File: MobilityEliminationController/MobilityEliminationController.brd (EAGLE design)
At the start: 57.1 x 63.5 mm, 97 parts, among them J11 M10X2, Q1 INFINEON_2N7002_DW, Q2 INFINEON_2N7002_DW, Q3 BS250F, Q4 BS250F, Q5 INFINEON_2N7002_DW, Q6 INFINEON_2N7002_DW, Q7 INFINEON_2N7002_DW, U1 MSP430F5521/5/7/9_PN80, U2 LTV-817, U3 SN74LV74, U4 SN74LV08

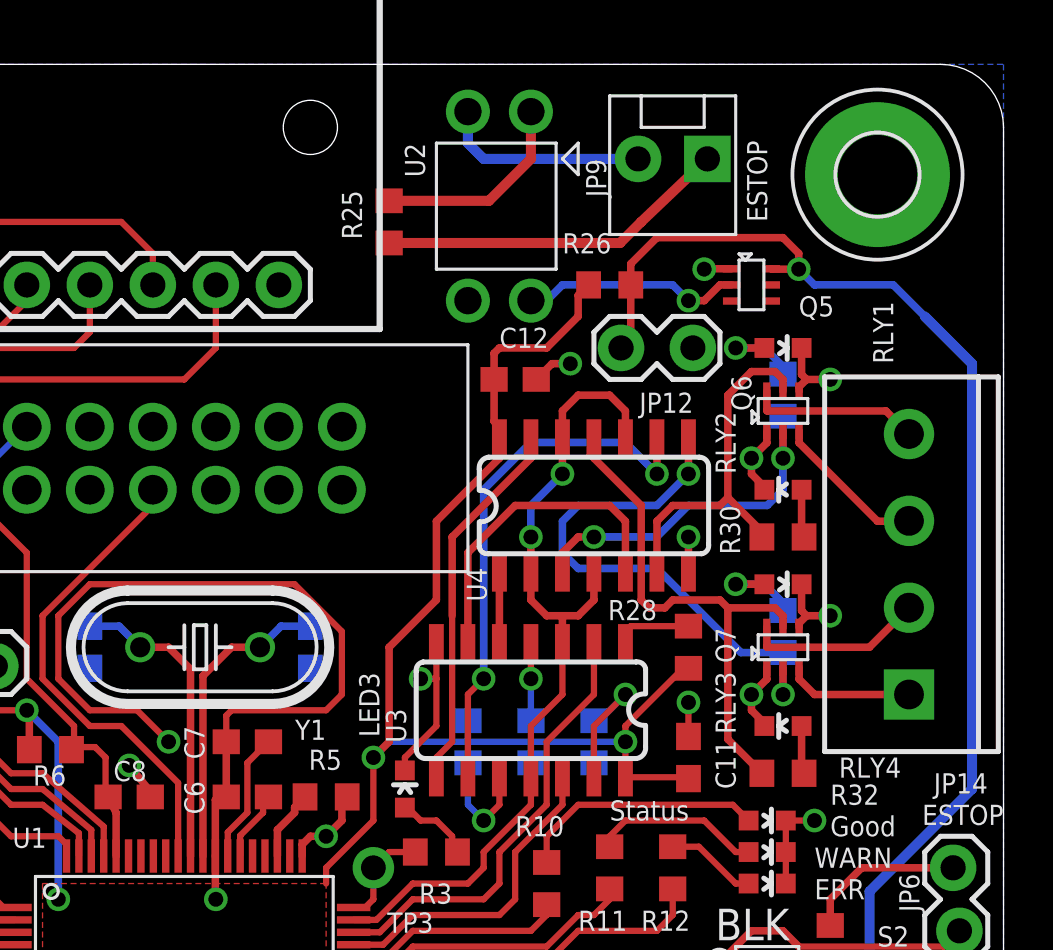
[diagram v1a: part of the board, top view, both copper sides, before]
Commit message: Power Controller, Elim-Mobility Controller, and PC2CAN sent to FAB
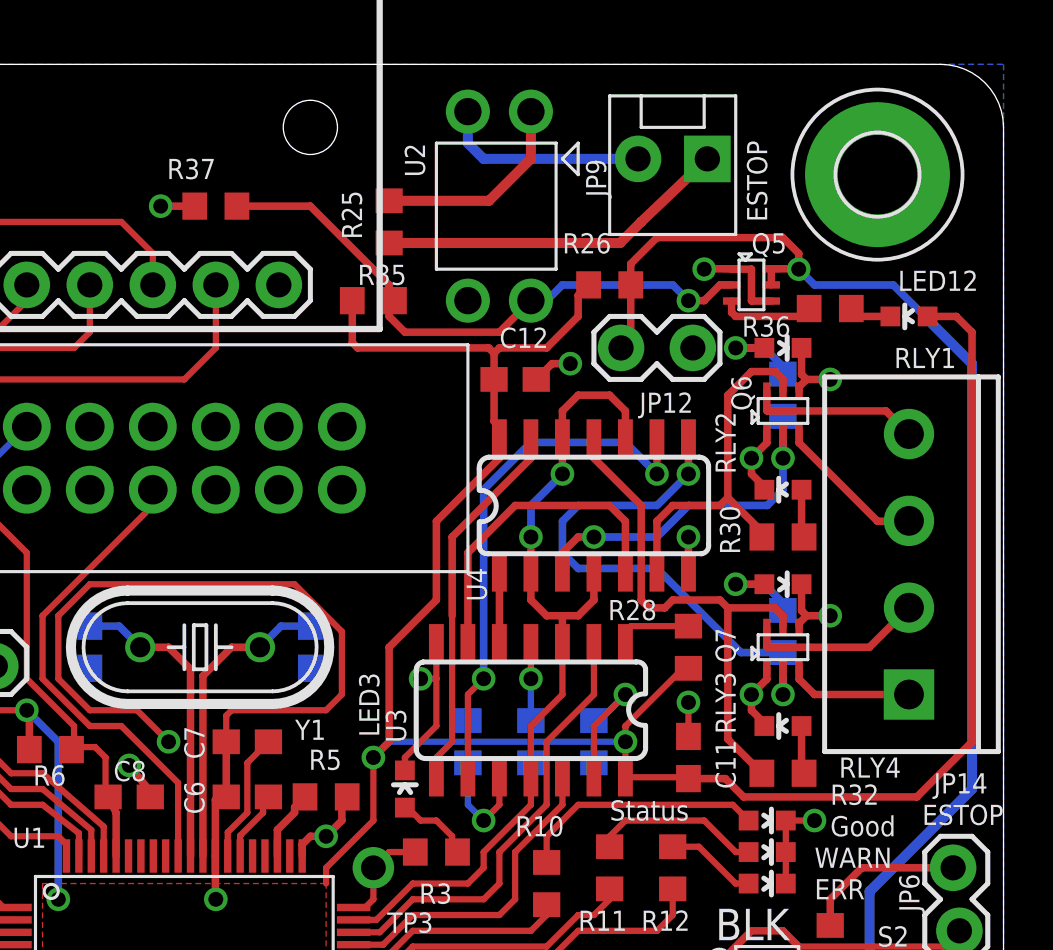
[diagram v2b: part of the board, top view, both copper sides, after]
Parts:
- added LED12: (no value), SparkFun-LED:LED-0603
- added R35: 10k, rcl:R0603
- added R36: 330, rcl:R0603
- added R37: 10M, rcl:R0603
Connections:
- new net N$15: Q5.3, R36.2
- new net N$16: LED12.C, R36.1
- net +3V3: now also LED12.A, R35.1
- net ESTOP_LOCAL: now also Q5.5
- net ESTOP_LOCAL_INV: now also R35.2, R37.1
- net GND: now also Q5.4, R37.2
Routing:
- net +3V3: track 162.1 -> 200.9 mm
- net ESTOP_LOCAL_INV: track 8.88 -> 24.4 mm
- net GND: track 111.5 -> 115.8 mm, vias 29 -> 30
- net N$15: track 0.00 -> 4.27 mm
- net N$16: track 0.00 -> 1.71 mm
- net ESTOP_LOCAL: track 138.2 -> 138.9 mm
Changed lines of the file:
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@@
 Controller</text>
 <text x="0.635" y="52.705" size="0.8128" layer="25">MCU RESET</text>
-<text x="52.705" y="51.435" size="0.8128" layer="25" rot="R90">RLY1</text>
+<text x="55.245" y="52.07" size="0.8128" layer="25" rot="R180">RLY1</text>
 <text x="46.355" y="46.99" size="0.8128" layer="25" rot="R90">RLY2</text>
 <text x="46.355" y="36.5125" size="0.8128" layer="25" rot="R90">RLY3</text>
@@
 <attribute name="VALUE" x="49.276" y="47.4345" size="0.4064" layer="27" rot="R180"/>
 </element>
-<element name="Q5" library="npol-discrete" package="INFINEON_SOT363" value="INFINEON_2N7002_DW" x="46.99" y="54.61" smashed="yes" rot="R270">
-<attribute name="NAME" x="48.895" y="53.34" size="0.8128" layer="25"/>
-</element>
 <element name="R26" library="rcl" package="R0603" value="10k" x="41.275" y="54.61" smashed="yes">
 <attribute name="NAME" x="39.37" y="55.88" size="0.8128" layer="25"/>
@@
 <element name="JP12" library="SparkFun-Connectors" package="1X02_LOCK" value="M02LOCK" x="41.91" y="52.07" smashed="yes">
 <attribute name="NAME" x="42.4688" y="49.4538" size="0.8128" layer="25" ratio="10"/>
+</element>
+<element name="Q5" library="npol-discrete" package="INFINEON_SOT363" value="INFINEON_2N7002_DW" x="46.99" y="54.61" smashed="yes" rot="R270">
+<attribute name="NAME" x="46.99" y="55.88" size="0.8128" layer="25"/>
+</element>
+<element name="R35" library="rcl" package="R0603" value="10k" x="31.75" y="53.975" smashed="yes">
+<attribute name="NAME" x="31.115" y="54.61" size="0.8128" layer="25"/>
+</element>
+<element name="R36" library="rcl" package="R0603" value="330" x="50.165" y="53.6575" smashed="yes" rot="R180">
+<attribute name="NAME" x="48.5775" y="53.34" size="0.8128" layer="25" rot="R180"/>
+</element>
+<element name="LED12" library="SparkFun-LED" package="LED-0603" value="" x="53.34" y="53.34" smashed="yes" rot="R90">
+<attribute name="NAME" x="56.134" y="55.1815" size="0.8128" layer="25" rot="R180"/>
+<attribute name="VALUE" x="54.356" y="54.4195" size="0.4064" layer="27" rot="R180"/>
+</element>
+<element name="R37" library="rcl" package="R0603" value="10M" x="25.4" y="57.785" smashed="yes" rot="R180">
+<attribute name="NAME" x="25.4" y="59.69" size="0.8128" layer="25" rot="R180"/>
 </element>
 </elements>
@@
 <wire x1="39.6875" y1="51.435" x2="38.95" y2="51.435" width="0.3048" layer="1"/>
 <wire x1="38.95" y1="51.435" x2="38.315" y2="50.8" width="0.3048" layer="1"/>
-<contactref element="Q5" pad="1"/>
 <contactref element="U2" pad="3"/>
 <contactref element="JP12" pad="2"/>
 <via x="45.085" y="55.245" extent="1-16" drill="0.6"/>
-<wire x1="46.19" y1="55.26" x2="45.1" y2="55.26" width="0.3048" layer="1"/>
 <wire x1="45.1" y1="55.26" x2="45.085" y2="55.245" width="0.3048" layer="1"/>
+<contactref element="Q5" pad="1"/>
+<contactref element="Q5" pad="4"/>
+<wire x1="46.19" y1="55.26" x2="45.085" y2="55.26" width="0.3048" layer="1"/>
+<wire x1="45.085" y1="55.26" x2="45.085" y2="55.245" width="0.3048" layer="1"/>
+<wire x1="47.79" y1="53.96" x2="47.005" y2="53.96" width="0.3048" layer="1"/>
+<wire x1="47.005" y1="53.96" x2="46.99" y2="53.975" width="0.3048" layer="1"/>
+<wire x1="46.99" y1="53.975" x2="46.99" y2="55.245" width="0.3048" layer="1"/>
+<wire x1="46.99" y1="55.245" x2="46.205" y2="55.245" width="0.3048" layer="1"/>
+<wire x1="46.205" y1="55.245" x2="46.19" y2="55.26" width="0.3048" layer="1"/>
+<contactref element="R37" pad="2"/>
+<via x="23.1775" y="57.785" extent="1-16" drill="0.6"/>
+<wire x1="24.55" y1="57.785" x2="23.1775" y2="57.785" width="0.3048" layer="1"/>
 </signal>
 <signal name="CAN_STBY">
@@
 <wire x1="40.005" y1="53.34" x2="40.005" y2="54.19" width="0.3048" layer="1"/>
 <wire x1="40.005" y1="54.19" x2="40.425" y2="54.61" width="0.3048" layer="1"/>
+<contactref element="R35" pad="1"/>
+<contactref element="LED12" pad="A"/>
+<wire x1="30.9" y1="53.975" x2="30.9" y2="52.285" width="0.3048" layer="1"/>
+<wire x1="30.9" y1="52.285" x2="31.115" y2="52.07" width="0.3048" layer="1"/>
+<wire x1="31.115" y1="52.07" x2="36.4" y2="52.07" width="0.3048" layer="1"/>
+<wire x1="36.4" y1="52.07" x2="36.615" y2="51.855" width="0.3048" layer="1"/>
+<wire x1="44.45" y1="34.71" x2="45.935" y2="34.71" width="0.3048" layer="1"/>
+<wire x1="45.935" y1="34.71" x2="46.6725" y2="33.9725" width="0.3048" layer="1"/>
+<wire x1="46.6725" y1="33.9725" x2="53.6575" y2="33.9725" width="0.3048" layer="1"/>
+<wire x1="53.6575" y1="33.9725" x2="55.88" y2="36.195" width="0.3048" layer="1"/>
+<wire x1="55.88" y1="36.195" x2="55.88" y2="52.705" width="0.3048" layer="1"/>
+<wire x1="55.88" y1="52.705" x2="55.245" y2="53.34" width="0.3048" layer="1"/>
+<wire x1="55.245" y1="53.34" x2="54.09" y2="53.34" width="0.3048" layer="1"/>
 </signal>
 <signal name="SBWTDIO">
@@
 <wire x1="46.99" y1="4.445" x2="47.625" y2="3.81" width="0.254" layer="16"/>
 <wire x1="47.625" y1="3.81" x2="47.625" y2="2.54" width="0.254" layer="16"/>
-<contactref element="Q5" pad="6"/>
 <contactref element="R26" pad="2"/>
 <contactref element="JP12" pad="1"/>
@@
 <wire x1="49.53" y1="54.61" x2="48.895" y2="55.245" width="0.3048" layer="16"/>
 <via x="48.895" y="55.245" extent="1-16" drill="0.6"/>
-<wire x1="48.895" y1="55.245" x2="47.805" y2="55.245" width="0.3048" layer="1"/>
-<wire x1="47.805" y1="55.245" x2="47.79" y2="55.26" width="0.3048" layer="1"/>
 <wire x1="42.125" y1="54.61" x2="42.125" y2="55.46" width="0.3048" layer="1"/>
 <wire x1="42.125" y1="55.46" x2="43.18" y2="56.515" width="0.3048" layer="1"/>
@@
 <wire x1="48.26" y1="56.515" x2="48.895" y2="55.88" width="0.3048" layer="1"/>
 <wire x1="48.895" y1="55.88" x2="48.895" y2="55.245" width="0.3048" layer="1"/>
+<contactref element="Q5" pad="6"/>
+<wire x1="47.79" y1="55.26" x2="48.895" y2="55.26" width="0.3048" layer="1"/>
+<wire x1="48.895" y1="55.26" x2="48.895" y2="55.245" width="0.3048" layer="1"/>
+<contactref element="Q5" pad="5"/>
+<wire x1="47.79" y1="55.26" x2="47.79" y2="54.61" width="0.3048" layer="1"/>
 </signal>
 <signal name="STEPPER_EN">
@@
 </signal>
 <signal name="ESTOP_LOCAL_INV">
-<contactref element="Q5" pad="2"/>
 <contactref element="U2" pad="4"/>
 <wire x1="38.1" y1="53.975" x2="38.735" y2="53.975" width="0.3048" layer="16"/>
@@
 <wire x1="44.45" y1="53.975" x2="45.085" y2="53.975" width="0.3048" layer="1"/>
 <wire x1="45.085" y1="53.975" x2="45.72" y2="54.61" width="0.3048" layer="1"/>
-<wire x1="45.72" y1="54.61" x2="46.19" y2="54.61" width="0.3048" layer="1"/>
+<contactref element="Q5" pad="2"/>
+<wire x1="46.19" y1="54.61" x2="45.72" y2="54.61" width="0.3048" layer="1"/>
+<contactref element="R35" pad="2"/>
+<wire x1="38.1" y1="53.975" x2="36.83" y2="52.705" width="0.3048" layer="1"/>
+<wire x1="36.83" y1="52.705" x2="33.02" y2="52.705" width="0.3048" layer="1"/>
+<wire x1="33.02" y1="52.705" x2="32.385" y2="53.34" width="0.3048" layer="1"/>
+<wire x1="32.385" y1="53.34" x2="32.385" y2="53.76" width="0.3048" layer="1"/>
+<wire x1="32.385" y1="53.76" x2="32.6" y2="53.975" width="0.3048" layer="1"/>
+<contactref element="R37" pad="1"/>
+<wire x1="32.385" y1="53.76" x2="32.385" y2="54.61" width="0.3048" layer="1"/>
+<wire x1="32.385" y1="54.61" x2="29.21" y2="57.785" width="0.3048" layer="1"/>
+<wire x1="29.21" y1="57.785" x2="26.25" y2="57.785" width="0.3048" layer="1"/>
 </signal>
 <signal name="N$13">
@@
 <wire x1="38.1" y1="59.69" x2="38.1" y2="61.595" width="0.4064" layer="1"/>
 </signal>
+<signal name="N$15">
+<contactref element="Q5" pad="3"/>
+<contactref element="R36" pad="2"/>
+<wire x1="46.19" y1="53.96" x2="46.19" y2="53.505" width="0.3048" layer="1"/>
+<wire x1="46.19" y1="53.505" x2="46.355" y2="53.34" width="0.3048" layer="1"/>
+<wire x1="46.355" y1="53.34" x2="49.53" y2="53.34" width="0.3048" layer="1"/>
+<wire x1="49.315" y1="53.6575" x2="49.315" y2="53.555" width="0.3048" layer="1"/>
+<wire x1="49.315" y1="53.555" x2="49.53" y2="53.34" width="0.3048" layer="1"/>
+</signal>
+<signal name="N$16">
+<contactref element="R36" pad="1"/>
+<contactref element="LED12" pad="C"/>
+<wire x1="52.59" y1="53.34" x2="51.3325" y2="53.34" width="0.3048" layer="1"/>
+<wire x1="51.3325" y1="53.34" x2="51.015" y2="53.6575" width="0.3048" layer="1"/>
+</signal>
 </signals>
